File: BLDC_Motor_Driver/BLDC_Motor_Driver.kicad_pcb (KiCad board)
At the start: 4 copper layers, 225.6 x 150.2 mm, 132 parts, among them J101 Conn_01x10, J102 395221002, J103 USB4105-GF-A, J104 Conn_01x05, J105 Conn_01x05, J106 Conn_01x04, J107 395221005, J108 395221003, J109 Conn_02x12_Counter_Clockwise, J110 395221005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

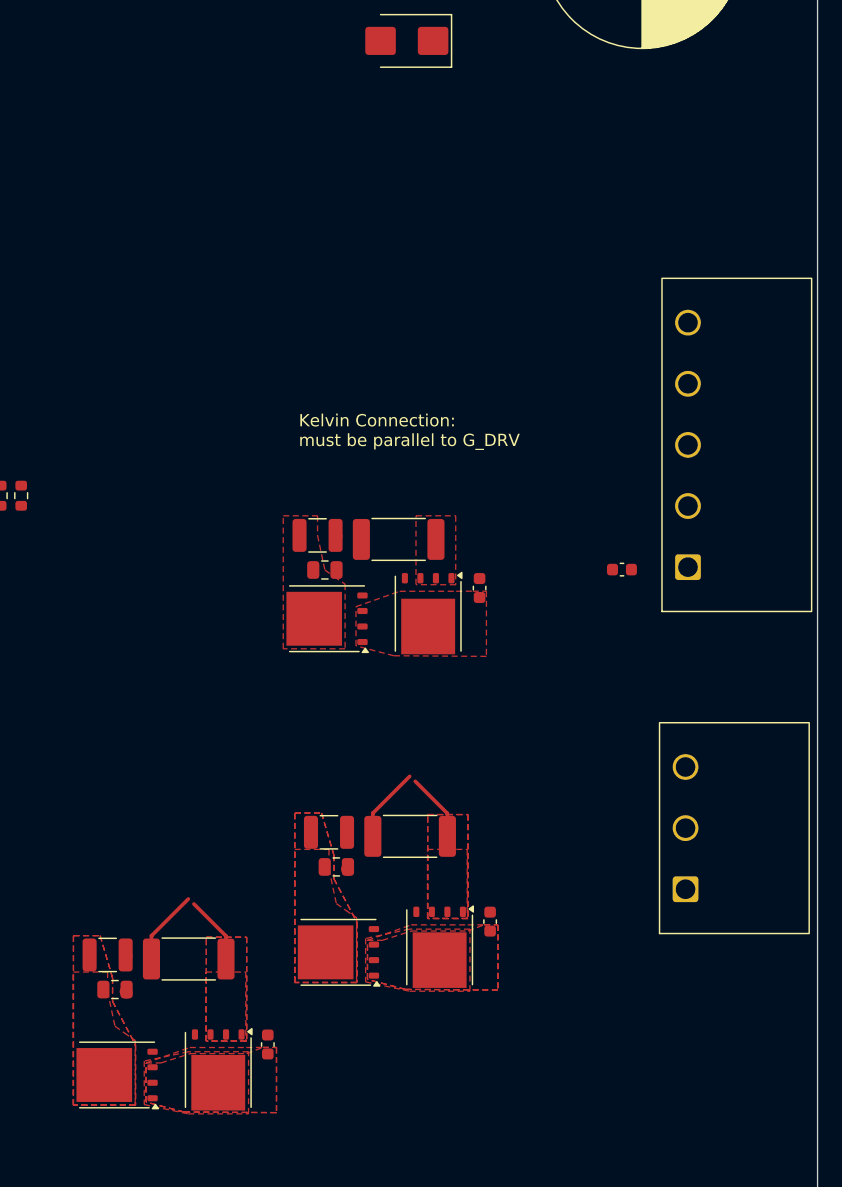
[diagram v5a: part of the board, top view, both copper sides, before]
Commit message: removed unnecessary Y phase. finished Motor Conn Layout
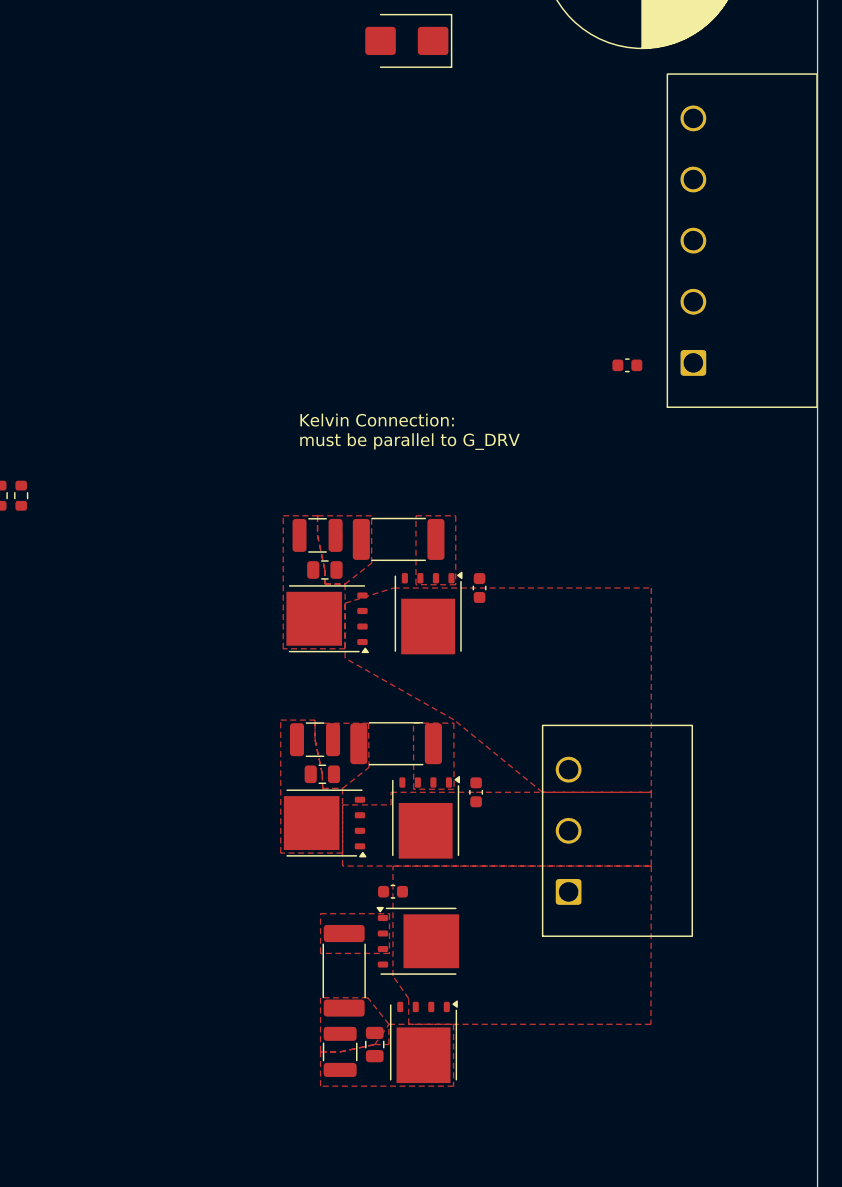
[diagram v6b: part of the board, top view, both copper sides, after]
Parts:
- D301: value 3.3V_LED -> RED LED
- D401: value FAULT_LED -> ORANGE_LED
- moved Q701 25.2 mm to (249.4, 116.4), turned to -90 degrees
- moved C701 21.7 mm to (245.4, 116.6), turned to 90 degrees
- moved C703 20.6 mm to (242.5, 117.2), turned to 90 degrees
- moved Q702 19.5 mm to (248.9, 108.2), turned to 0 degrees
- moved C101 16.7 mm to (266.0, 61.0)
- moved J107 16.7 mm to (271.4, 60.8)
- moved C702 16.2 mm to (246.9, 104.1), turned to 180 degrees
- moved R701 12.8 mm to (242.9, 110.6), turned to -90 degrees
- moved C602 10.6 mm to (253.7, 96.0)
- moved Q601 10.6 mm to (241.3, 98.5)
- moved Q602 10.6 mm to (249.5, 98.1)
- moved J108 9.57 mm to (261.2, 104.1)
- moved R601 7.66 mm to (247.1, 92.0)
- moved C601 7.66 mm to (241.1, 94.5)
- moved C603 7.66 mm to (240.5, 91.7)
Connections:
- J107 pad 2: /HALL_U_CONN -> /HALL_W_CONN
- J107 pad 4: /HALL_W_CONN -> /HALL_U_CONN
- J108 pad 1: /MOTOR_U -> /MOTOR_W
- J108 pad 3: /MOTOR_W -> /MOTOR_U
- U401 pad 29: /Gate-Driver/BS_Y -> unconnected-(U401-BS_Y2-Pad29)
- U401 pad 30: /Gate-Driver/HS_Y -> unconnected-(U401-HS_Y2-Pad30)
- U401 pad 31: /Gate-Driver/MOTOR_Y -> unconnected-(U401-BM_Y2-Pad31)
- U401 pad 32: /Gate-Driver/LS_Y -> unconnected-(U401-LS_Y2-Pad32)
- U401 pad 33: /Gate-Driver/CSP_Y -> unconnected-(U401-CSP3-Pad33)
- U401 pad 34: GND -> unconnected-(U401-CSN3-Pad34)
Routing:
- net GND: track 12.8 -> 0.21 mm
- net /Gate-Driver/CSP_W: track 5.59 -> 0.00 mm
- net /Gate-Driver/CSP_V: track 5.59 -> 0.00 mm
- removed copper zone on F.Cu, net (none)

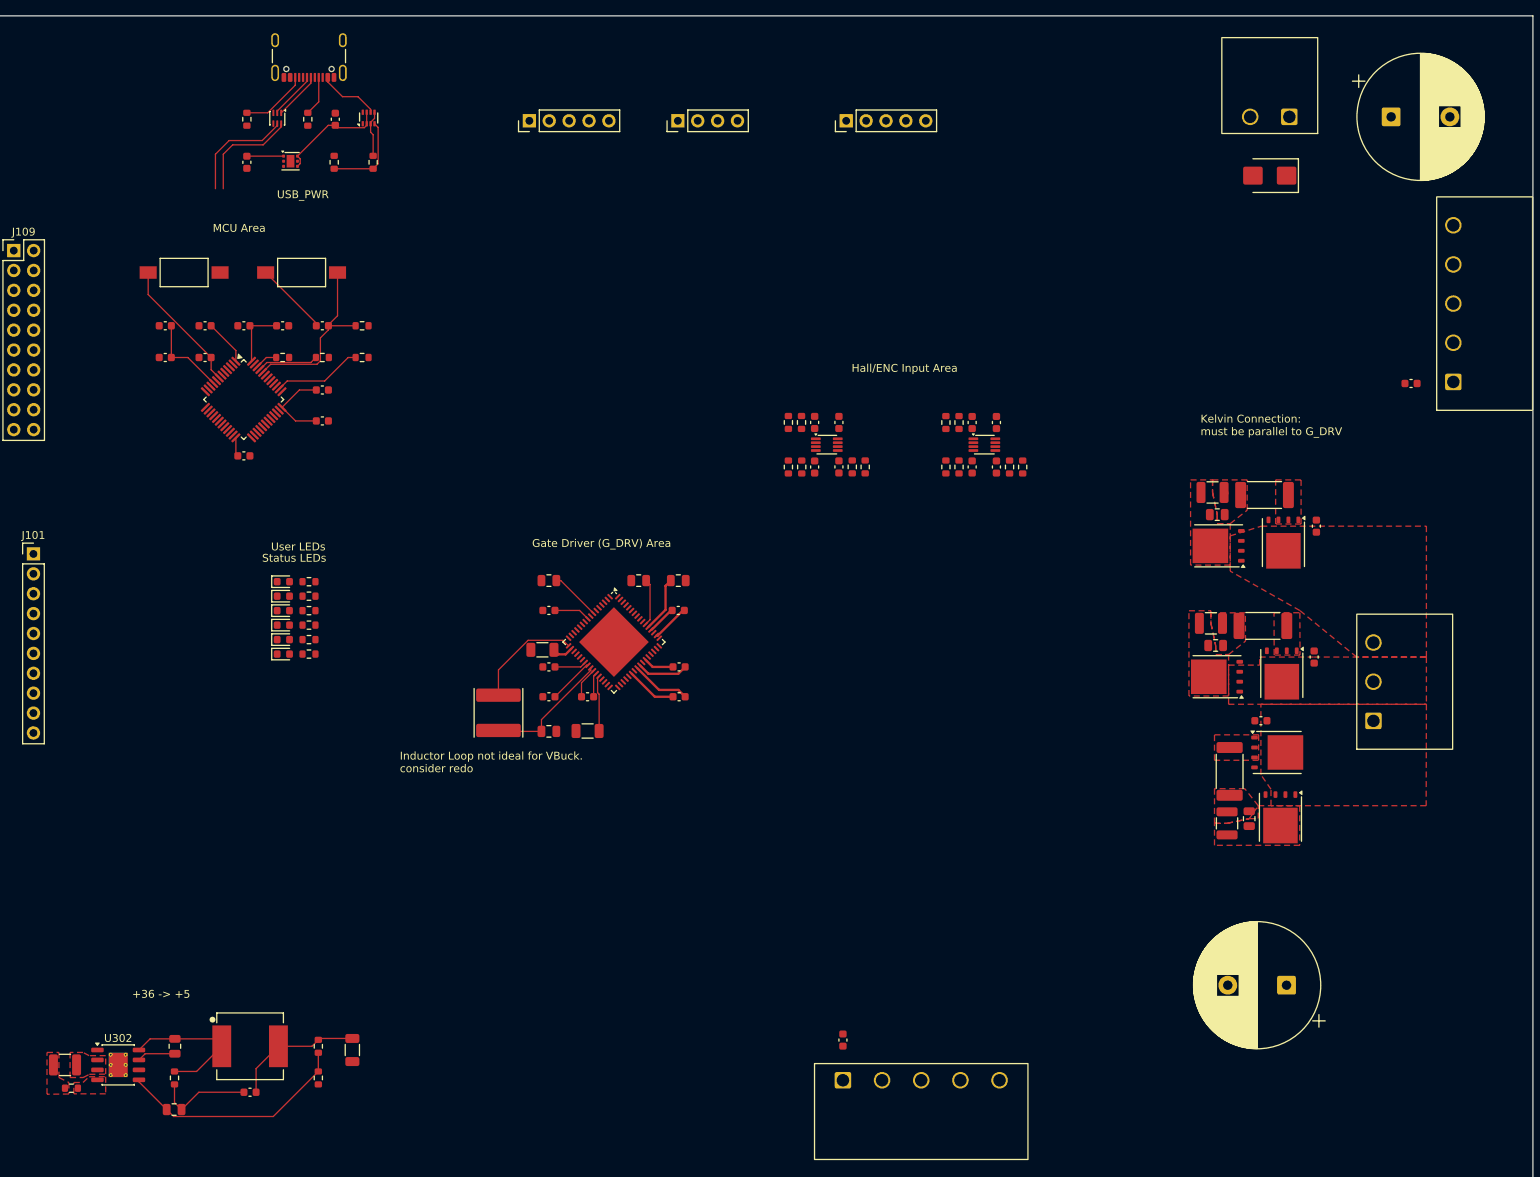
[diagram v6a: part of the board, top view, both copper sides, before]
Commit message: changed rst/en pullups to 3V3, rerouted 5V regulator
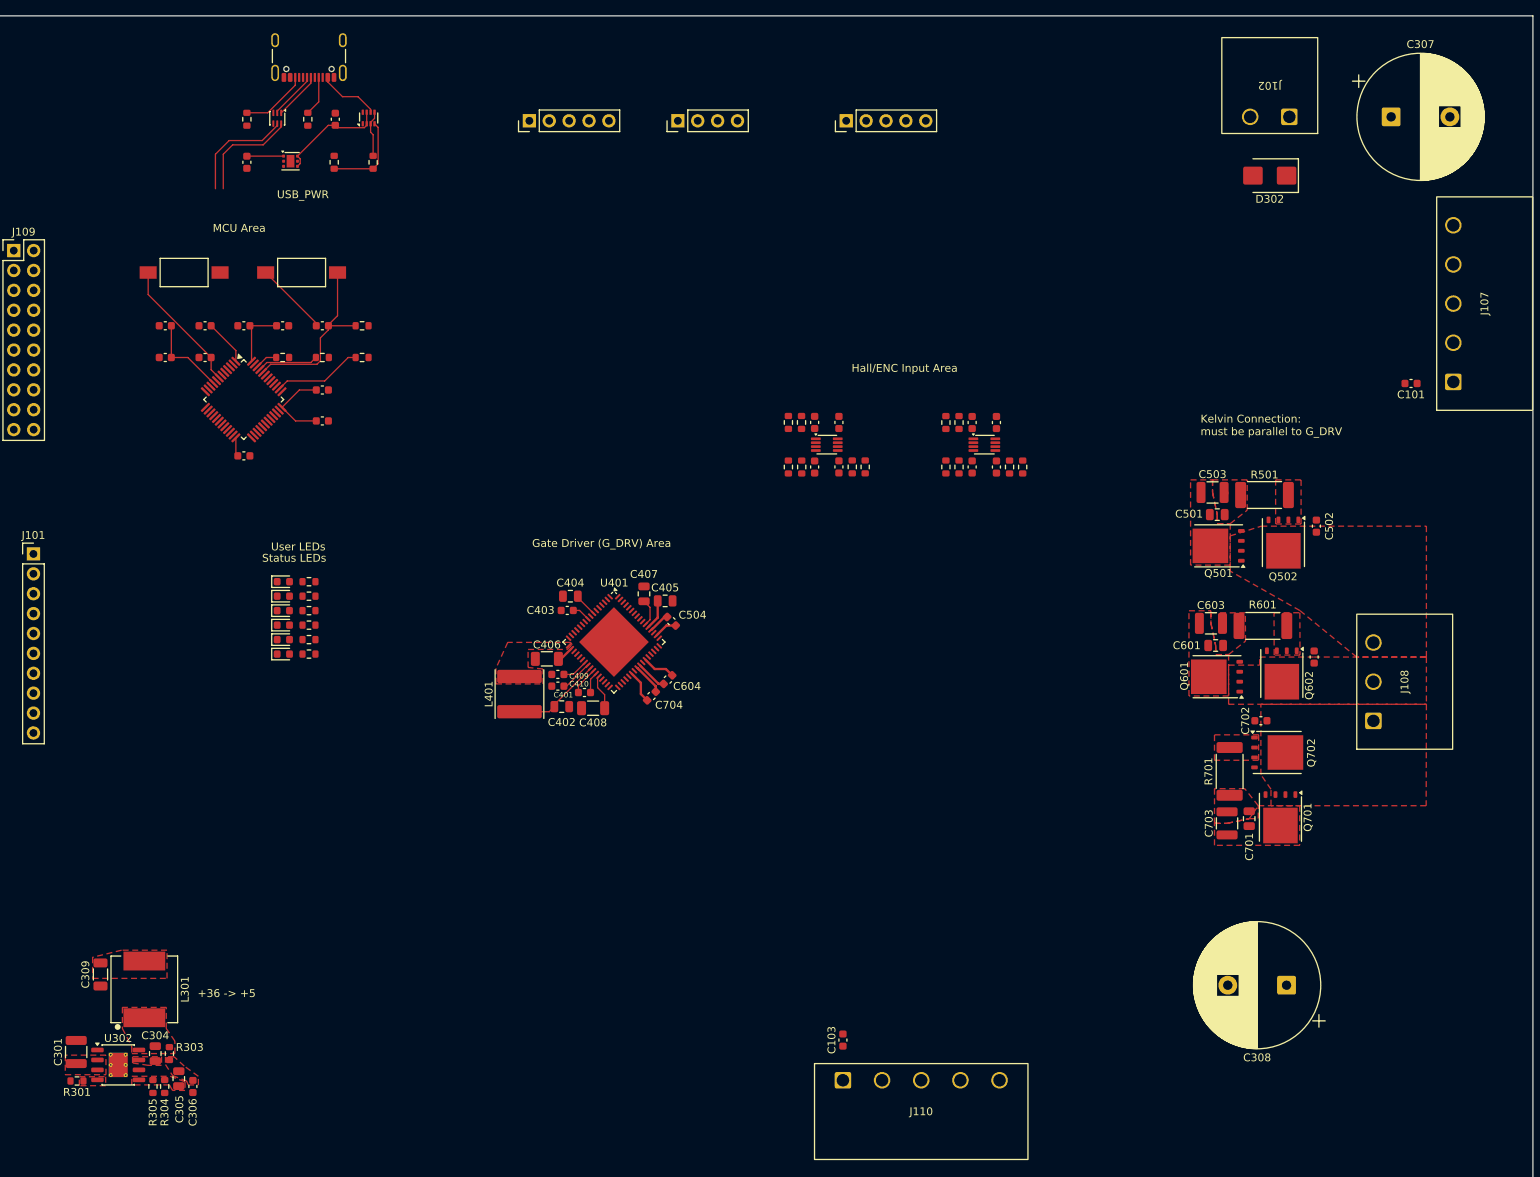
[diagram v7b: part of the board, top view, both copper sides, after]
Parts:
- moved C309 33.6 mm to (98.7, 136.5)
- moved R305 21.1 mm to (105.4, 150.8)
- moved R304 20.3 mm to (106.9, 150.8), turned to 90 degrees
- moved L301 15.3 mm to (104.3, 138.4), turned to 90 degrees
- moved C306 7.33 mm to (110.5, 150.8), turned to -90 degrees
- moved C305 3.99 mm to (108.7, 149.8), turned to -90 degrees
- moved L401 3.59 mm to (152.2, 100.7)
- moved C402 3.56 mm to (157.6, 102.3)
- moved C704 3.53 mm to (169.1, 100.9), turned to -135 degrees
- moved C404 3.39 mm to (158.7, 88.2)
- moved R303 3.18 mm to (107.5, 146.6)
- moved C405 3.09 mm to (170.8, 88.8)
- moved C408 2.99 mm to (161.6, 102.5)
- moved C304 2.67 mm to (105.7, 146.6)
- moved C403 2.34 mm to (158.3, 90.0)
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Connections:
- R401 pad 1: +36V -> +3V3
- R402 pad 1: +36V -> +3V3
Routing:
- net Net-(U302-FB): track 29.8 -> 0.00 mm
- net Net-(U302-SW): track 18.9 -> 0.00 mm
- net /5V_REG: track 22.8 -> 5.91 mm
- net /Gate-Driver/DRIVER_SW: track 14.0 -> 0.00 mm
- net Net-(C305-Pad1): track 12.5 -> 0.00 mm
- net Net-(U302-BST): track 4.92 -> 0.02 mm
- net +36V: track 9.90 -> 6.05 mm
- net /Gate-Driver/BS_W: track 7.65 -> 4.04 mm
- net /DRIVER_V_{BUCK}: track 16.2 -> 12.8 mm
- net +1V8: track 6.48 -> 3.02 mm
- net /Gate-Driver/BS_V: track 6.59 -> 3.81 mm
- net /Gate-Driver/DRIVER_V_{DRV}: track 7.14 -> 4.52 mm
- net /Gate-Driver/DRIVER_A1V8: track 6.04 -> 3.51 mm
- net +3V3: track 56.3 -> 54.0 mm
- net /MOTOR_W: track 6.52 -> 4.25 mm
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- added copper zone on F.Cu, net /5V_REG
- added copper zone on F.Cu, net /Gate-Driver/DRIVER_SW
- added copper zone on F.Cu, net Net-(C305-Pad1)
- added copper zone on F.Cu, net Net-(U302-BST)
- added copper zone on F.Cu, net Net-(U302-FB)
- added copper zone on F.Cu, net Net-(U302-SW)
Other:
- board text removed: "Inductor Loop not ideal for VBuck. consider redo"
